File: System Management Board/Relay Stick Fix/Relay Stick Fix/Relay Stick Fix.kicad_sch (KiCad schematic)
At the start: 9 parts, among them J1 Conn_02x04, Q1 NMOS

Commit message: pwr routed, test points etc
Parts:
- added D1: LED GRN, LED_SMD:LED_1206_3216Metric_Pad1.42x1.75mm_HandSolder, symbol Device:LED
- added D2: LED RED, LED_SMD:LED_1206_3216Metric_Pad1.42x1.75mm_HandSolder, symbol Device:LED
- added R4, R5: 220, Resistor_SMD:R_1206_3216Metric_Pad1.30x1.75mm_HandSolder, symbol Device:R
- added TP1, TP2: TestPoint, TestPoint:TestPoint_Pad_D1.0mm, symbol Connector:TestPoint
- added TP3, TP4: TestPoint, TestPoint:TestPoint_THTPad_D1.0mm_Drill0.5mm, symbol Connector:TestPoint
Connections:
- net 5V Bootstrap: now also D1.2 (A)
- net Fault: now also D2.2 (A)
- net GND: now also R4.2, R5.2
- net Gate: now also Q1.4 (G), R2.2, TP2.1
- net Vbat Prot: now also TP3.1
- net i3: now also TP4.1
- net Driver Out: now reaches R2.1, U1.8 (GATE)
- net Driver Out: now also TP1.1
- new net: D2.1 (K), R5.1
- new net: D1.1 (K), R4.1
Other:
- moved on the sheet: C1, H1, Q1, R1, R2, R3

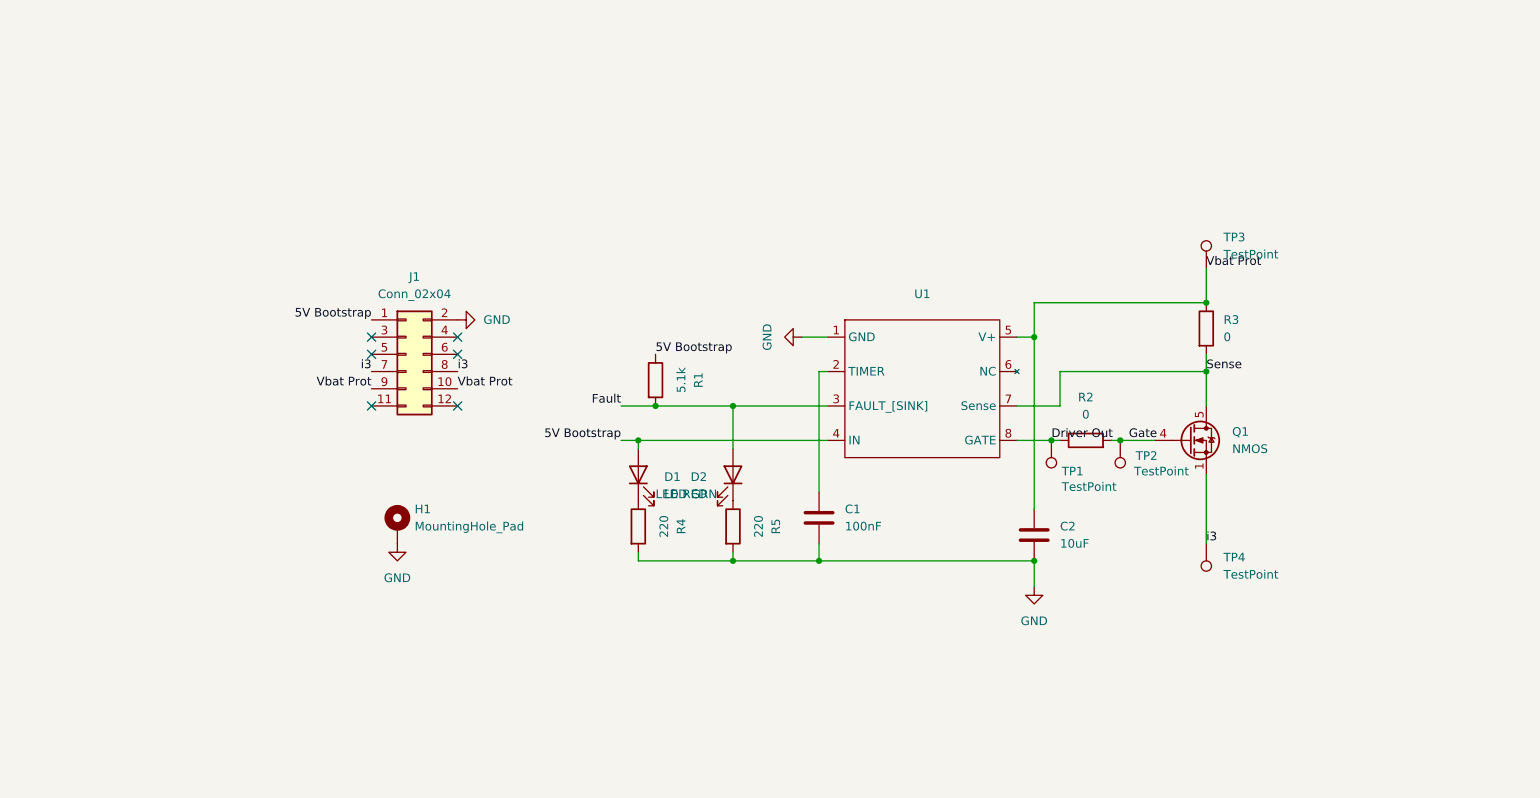
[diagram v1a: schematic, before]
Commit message: schematic redability improved
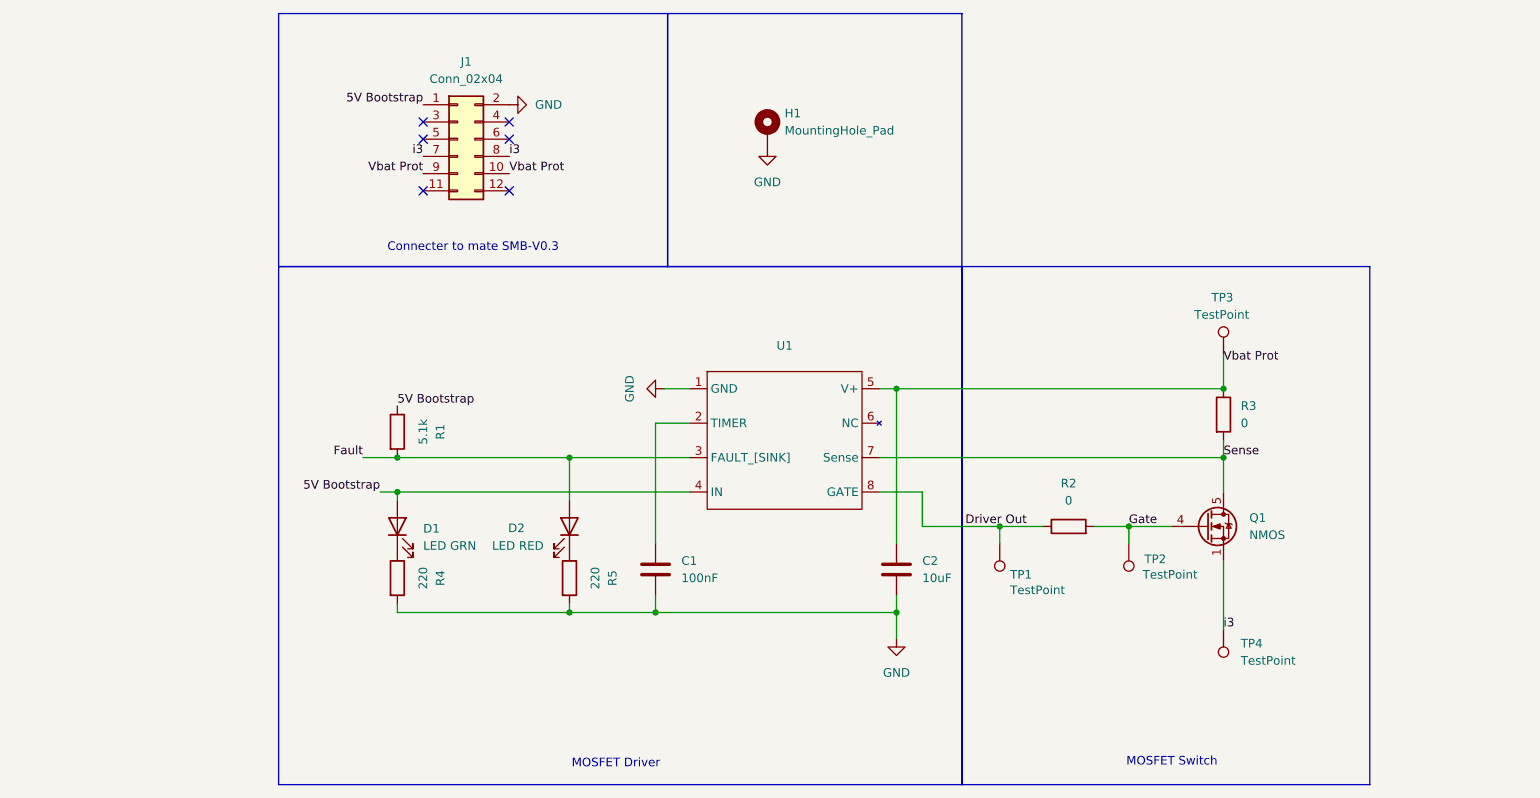
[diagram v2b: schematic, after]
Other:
- note added: "Connecter to mate SMB-V0.3"
- note added: "MOSFET Driver"
- note added: "MOSFET Switch"
- moved on the sheet: C1, C2, D1, D2, H1, J1, Q1, R1, R2, R3, R4, R5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

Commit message: capacitor footprint correction 1210
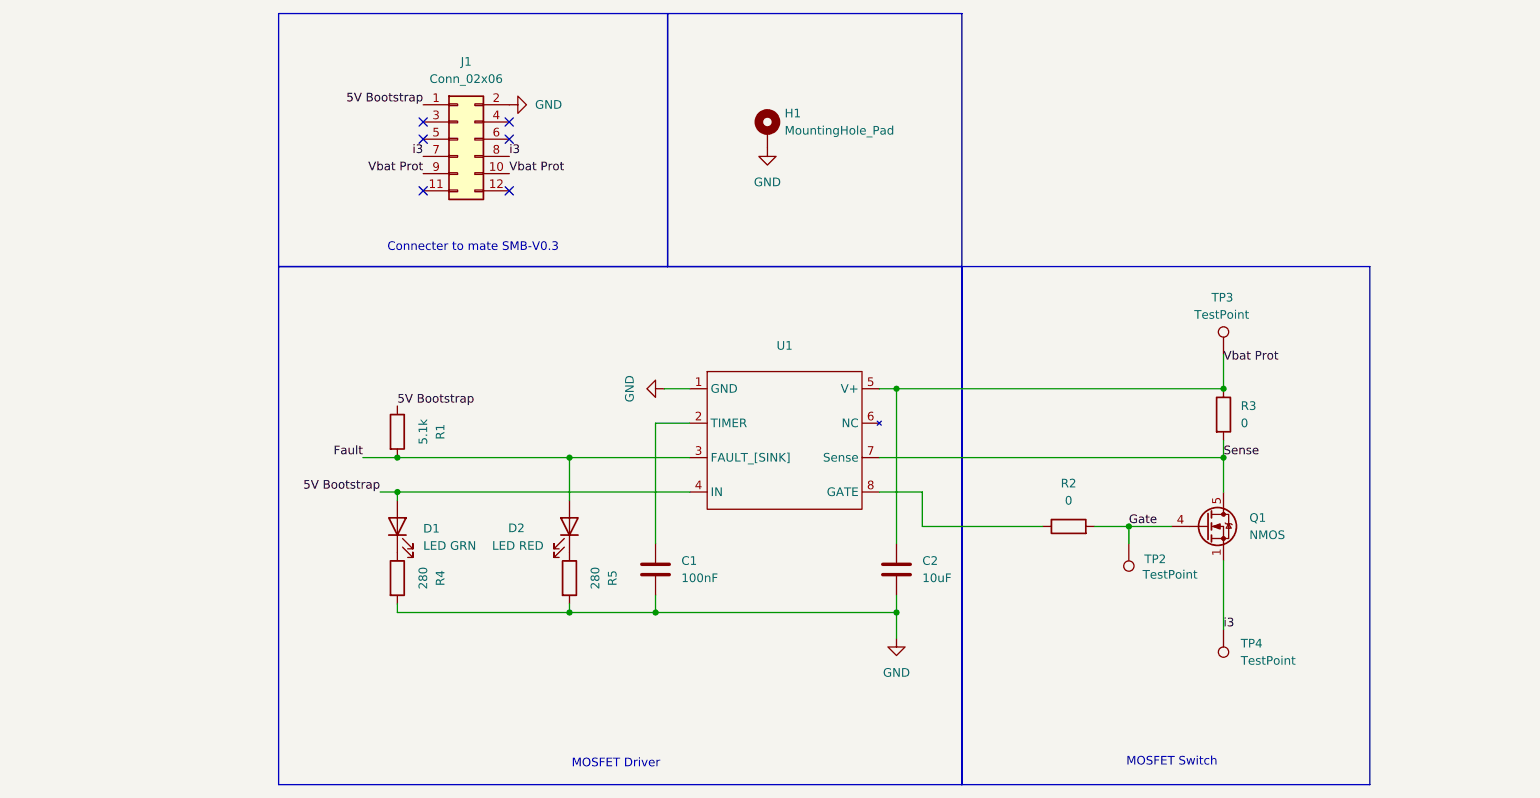
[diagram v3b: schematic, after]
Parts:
- removed TP1: TestPoint, TestPoint:TestPoint_Pad_D1.0mm, symbol Connector:TestPoint
- C2: footprint Capacitor_SMD:C_1206_3216Metric_Pad1.33x1.80mm_HandSolder -> Capacitor_SMD:C_1210_3225Metric_Pad1.33x2.70mm_HandSolder
- J1: value Conn_02x04 -> Conn_02x06
- R4, R5: value 220 -> 280
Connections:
- net Driver Out: no longer names the net of R2.1, U1.8 (GATE)
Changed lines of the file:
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@@
-	)
-	(junction
-		(at 199.39 114.3)
-		(diameter 0)
-		(color 0 0 0 0)
 	)
 	(junction
@@
 	(wire
 		(pts
-			(xy 199.39 114.3) (xy 187.96 114.3)
+			(xy 187.96 114.3) (xy 205.74 114.3)
 		)
 		(stroke
@@
 	(wire
 		(pts
-			(xy 199.39 116.84) (xy 199.39 114.3)
-		)
-		(stroke
-			(width 0)
-			(type default)
-		)
-	)
-	(wire
-		(pts
 			(xy 181.61 104.14) (xy 232.41 104.14)
 		)
@@
 		(pts
 			(xy 232.41 88.9) (xy 232.41 93.98)
-		)
-		(stroke
-			(width 0)
-			(type default)
-		)
-	)
-	(wire
-		(pts
-			(xy 205.74 114.3) (xy 199.39 114.3)
 		)
 		(stroke
@@
 			)
 			(justify right bottom)
-		)
-	)
-	(label "Driver Out"
-		(at 194.31 114.3 0)
-		(fields_autoplaced yes)
-		(effects
-			(font
-				(size 1.27 1.27)
-			)
-			(justify left bottom)
 		)
 	)
@@
 			)
 		)
-		(property "Value" "220"
+		(property "Value" "280"
 			(at 139.7 121.92 90)
 			(effects
@@
 			)
 		)
-		(property "Value" "220"
+		(property "Value" "280"
 			(at 114.3 121.92 90)
 			(effects
@@
 			)
 		)
-		(property "Footprint" "Capacitor_SMD:C_1206_3216Metric_Pad1.33x1.80mm_HandSolder"
+		(property "Footprint" "Capacitor_SMD:C_1210_3225Metric_Pad1.33x2.70mm_HandSolder"
 			(at 185.1152 124.46 0)
 			(effects
@@
 				(path "/8d33c889-5d8e-4500-89a6-789bc0f250c8"
 					(reference "R2")
-					(unit 1)
-				)
-			)
-		)
-	)
-	(symbol
-		(lib_id "Connector:TestPoint")
-		(at 199.39 116.84 180)
-		(unit 1)
-		(exclude_from_sim no)
-		(in_bom yes)
-		(on_board yes)
-		(dnp no)
-		(property "Reference" "TP1"
-			(at 200.914 121.412 0)
-			(effects
-				(font
-					(size 1.27 1.27)
-				)
-				(justify right)
-			)
-		)
-		(property "Value" "TestPoint"
-			(at 200.914 123.698 0)
-			(effects
-				(font
-					(size 1.27 1.27)
-				)
-				(justify right)
-			)
-		)
-		(property "Footprint" "TestPoint:TestPoint_Pad_D1.0mm"
-			(at 194.31 116.84 0)
-			(effects
-				(font
-					(size 1.27 1.27)
-				)
-				(hide yes)
-			)
-		)
-		(property "Datasheet" "~"
-			(at 194.31 116.84 0)
-			(effects
-				(font
-					(size 1.27 1.27)
-				)
-				(hide yes)
-			)
-		)
-		(property "Description" "test point"
-			(at 199.39 116.84 0)
-			(effects
-				(font
-					(size 1.27 1.27)
-				)
-				(hide yes)
-			)
-		)
-		(pin "1"
-		)
-		(instances
-			(project "Relay Stick Fix"
-				(path "/8d33c889-5d8e-4500-89a6-789bc0f250c8"
-					(reference "TP1")
 					(unit 1)
 				)
@@
 			)
 		)
-		(property "Value" "Conn_02x04"
+		(property "Value" "Conn_02x06"
 			(at 120.65 48.26 0)
 			(effects

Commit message: implementing mark's notes
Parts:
- added U2: 74LVC1G04, Package_TO_SOT_SMD:SOT-23-5, symbol 74xGxx:74LVC1G04
- C1: value 100nF -> 0.1uF
- R3: value 0 -> .001
- R4, R5: value 280 -> 1k
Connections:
- net 5V Bootstrap: now also U2.5 (VCC)
- net Fault: now also U2.2; no longer D2.2 (A)
- net GND: now also U2.3 (GND)
- net Sense: now also U1.6 (Sense); no longer U1.7 (Sense)
- net Vbat Prot: now also U1.8 (V+); no longer U1.5 (V+)
- net at R2.1: now also U1.5 (GATE); no longer U1.8 (GATE)
- new net: D2.2 (A), U2.4
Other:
- note added: "Fault pin pulls active LOW when overcurrent protection activates"
- note added: "Over current sensing and shutdown is triggered by a 65mV voltage drop w.r.t the supply. I = 65mV / R3 65A = 65mV / 0.001 Ohm"
- moved on the sheet: D1, D2, R1, R4, R5

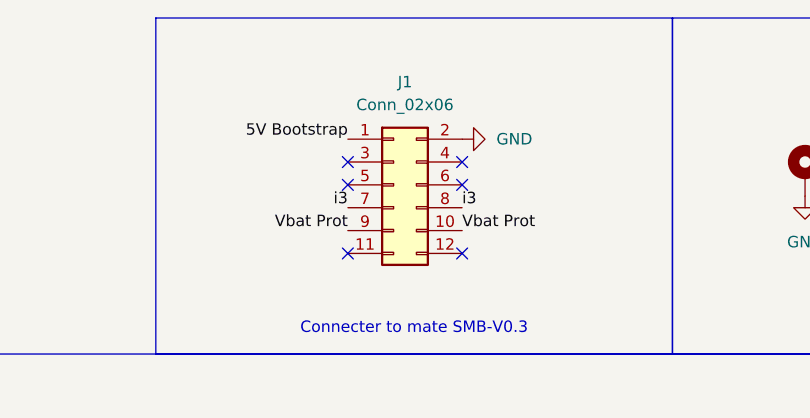
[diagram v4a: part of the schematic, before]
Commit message: fixed a mjor issue where 5V boot strap and GND headers were reversed
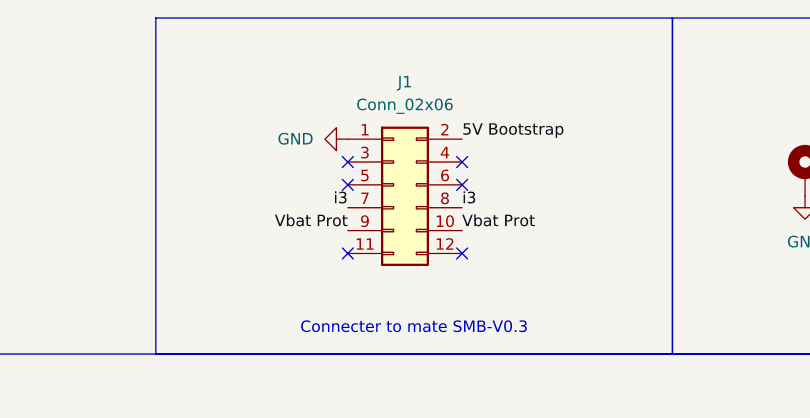
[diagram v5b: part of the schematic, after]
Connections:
- net 5V Bootstrap: now also J1.2 (Pin_2); no longer J1.1 (Pin_1)
- net GND: now also J1.1 (Pin_1); no longer J1.2 (Pin_2)
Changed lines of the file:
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@@
-		)
-	)
-	(label "5V Bootstrap"
-		(at 114.3 52.07 180)
-		(fields_autoplaced yes)
-		(effects
-			(font
-				(size 1.27 1.27)
-			)
-			(justify right bottom)
 		)
 	)
@@
 		)
 	)
+	(label "5V Bootstrap"
+		(at 127 52.07 0)
+		(fields_autoplaced yes)
+		(effects
+			(font
+				(size 1.27 1.27)
+			)
+			(justify left bottom)
+		)
+	)
 	(symbol
 		(lib_id "Device:C")
@@
 	(symbol
 		(lib_id "power:GND")
+		(at 114.3 52.07 270)
+		(unit 1)
+		(exclude_from_sim no)
+		(in_bom yes)
+		(on_board yes)
+		(dnp no)
+		(fields_autoplaced yes)
+		(property "Reference" "#PWR02"
+			(at 107.95 52.07 0)
+			(effects
+				(font
+					(size 1.27 1.27)
+				)
+				(hide yes)
+			)
+		)
+		(property "Value" "GND"
+			(at 110.49 52.0699 90)
+			(effects
+				(font
+					(size 1.27 1.27)
+				)
+				(justify right)
+			)
+		)
+		(property "Footprint" ""
+			(at 114.3 52.07 0)
+			(effects
+				(font
+					(size 1.27 1.27)
+				)
+				(hide yes)
+			)
+		)
+		(property "Datasheet" ""
+			(at 114.3 52.07 0)
+			(effects
+				(font
+					(size 1.27 1.27)
+				)
+				(hide yes)
+			)
+		)
+		(property "Description" "Power symbol creates a global label with name \"GND\" , ground"
+			(at 114.3 52.07 0)
+			(effects
+				(font
+					(size 1.27 1.27)
+				)
+				(hide yes)
+			)
+		)
+		(pin "1"
+		)
+		(instances
+			(project "Relay Stick Fix"
+				(path "/8d33c889-5d8e-4500-89a6-789bc0f250c8"
+					(reference "#PWR02")
+					(unit 1)
+				)
+			)
+		)
+	)
+	(symbol
+		(lib_id "power:GND")
 		(at 165.1 58.42 0)
 		(unit 1)
@@
 					(unit 1)
 				)
-			)
-		)
-	)
-	(symbol
-		(lib_id "power:GND")
-		(at 127 52.07 90)
-		(unit 1)
-		(exclude_from_sim no)
-		(in_bom yes)
-		(on_board yes)
-		(dnp no)
-		(fields_autoplaced yes)
-		(property "Reference" "#PWR02"
-			(at 133.35 52.07 0)
-			(effects
-				(font
-					(size 1.27 1.27)
-				)
-				(hide yes)
-			)
-		)
-		(property "Value" "GND"
-			(at 130.81 52.0699 90)
-			(effects
-				(font
-					(size 1.27 1.27)
-				)
-				(justify right)
-			)
-		)
-		(property "Footprint" ""
-			(at 127 52.07 0)
-			(effects
-				(font
-					(size 1.27 1.27)
-				)
-				(hide yes)
-			)
-		)
-		(property "Datasheet" ""
-			(at 127 52.07 0)
-			(effects
-				(font
-					(size 1.27 1.27)
-				)
-				(hide yes)
-			)
-		)
-		(property "Description" "Power symbol creates a global label with name \"GND\" , ground"
-			(at 127 52.07 0)
-			(effects
-				(font
-					(size 1.27 1.27)
-				)
-				(hide yes)
-			)
-		)
-		(pin "1"
-		)
-		(instances
-			(project "Relay Stick Fix"
-				(path "/8d33c889-5d8e-4500-89a6-789bc0f250c8"
-					(reference "#PWR02")
-					(unit 1)
-				)
